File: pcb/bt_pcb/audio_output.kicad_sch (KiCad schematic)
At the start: 37 parts, among them J16 ReanNYS216G, J17 ReanNYS216G, U3 MCP6004

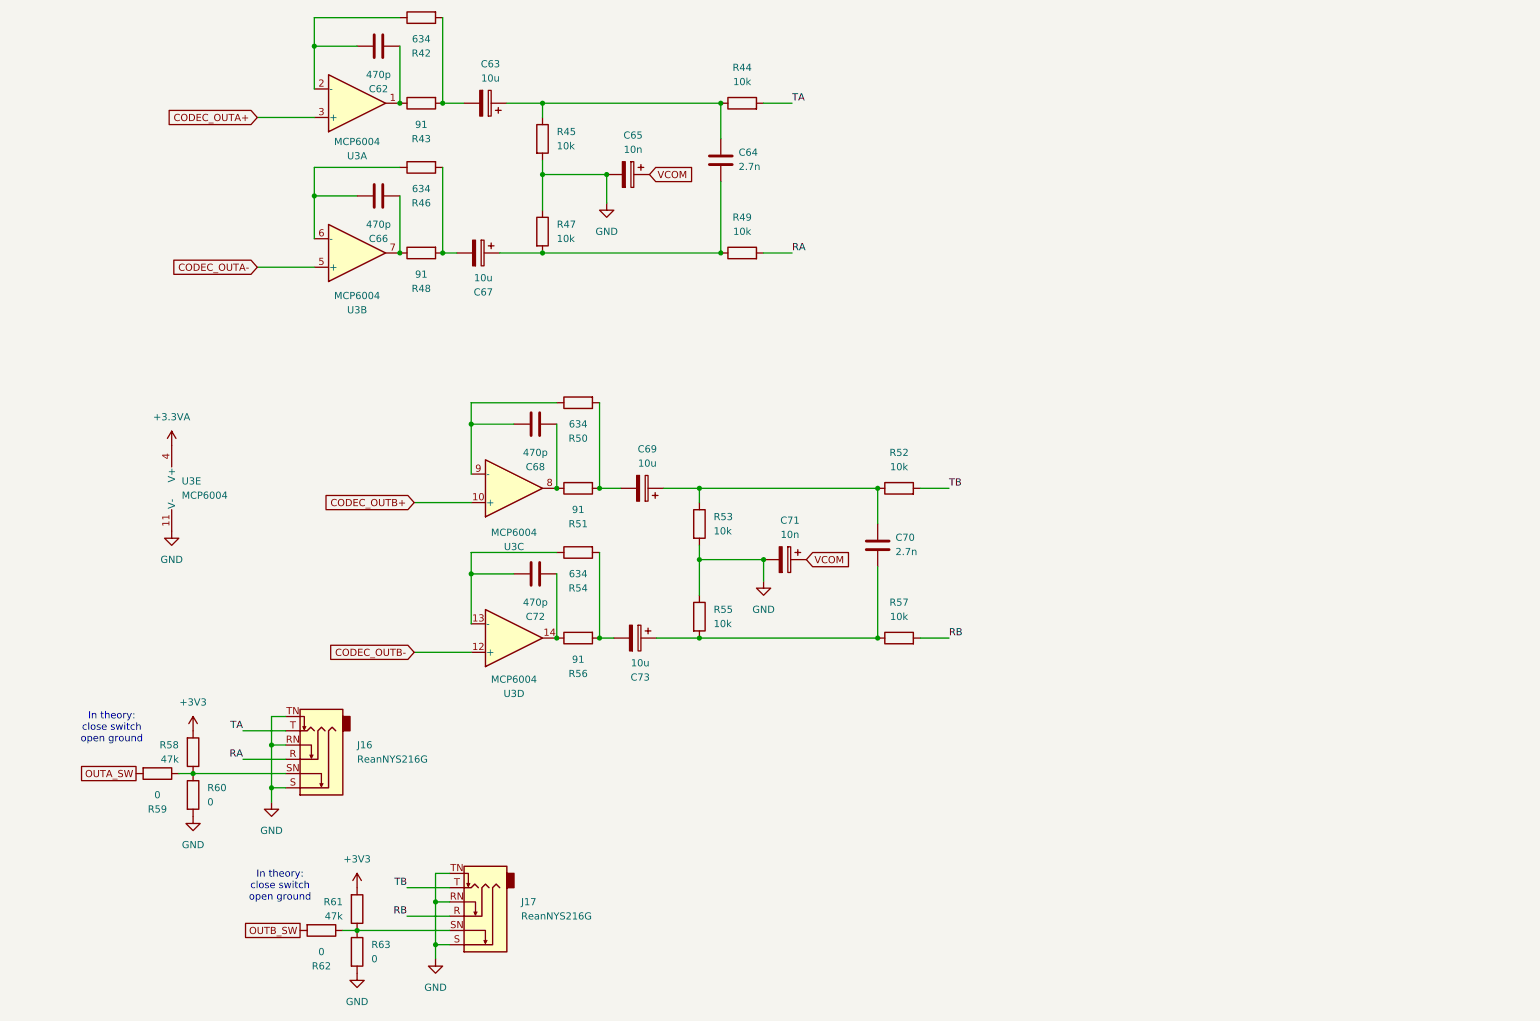
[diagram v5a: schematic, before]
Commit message: pcb with some schematic tuning
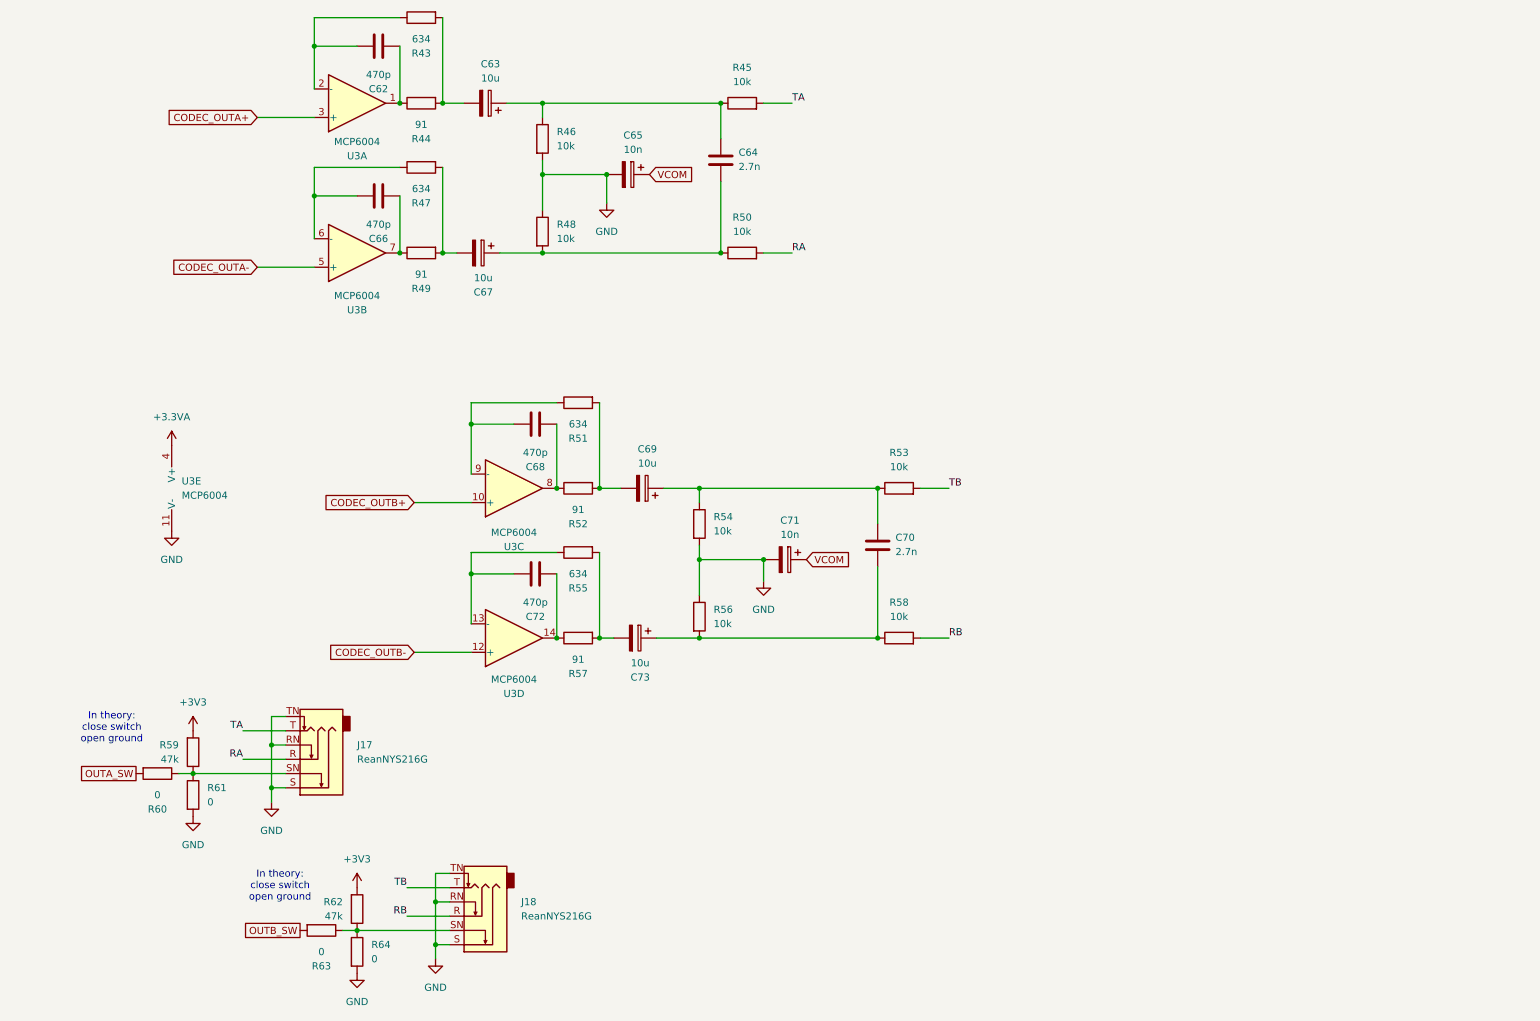
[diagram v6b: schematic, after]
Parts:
- renumbered J16 to J17, J17 to J18, R42 to R43, R43 to R44, R44 to R45, R45 to R46, R46 to R47, R47 to R48, R48 to R49, R49 to R50, R50 to R51, R51 to R52, R52 to R53, R53 to R54, R54 to R55, R55 to R56, R56 to R57, R57 to R58, R58 to R59, R59 to R60, R60 to R61, R61 to R62, R62 to R63, R63 to R64

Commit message: pcb now under revision
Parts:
- R46: renamed from R45; value 10k -> 470
- R51: renamed from R50; value 10k -> 470
- R54: renamed from R53; value 10k -> 470
- R59: renamed from R58; value 10k -> 470
- renumbered C62 to C66, C63 to C67, C64 to C68, C65 to C69, C66 to C70, C67 to C71, C68 to C72, C69 to C73, C70 to C74, C71 to C75, C72 to C76, C73 to C77, R43 to R44, R44 to R45, R46 to R47, R47 to R48, R48 to R49, R49 to R50, R51 to R52, R52 to R53, R54 to R55, R55 to R56, R56 to R57, R57 to R58, R59 to R60, R60 to R61, R61 to R62, R62 to R63, R63 to R64, R64 to R65

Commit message: first notes
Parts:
- renumbered C66 to C56, C67 to C57, C68 to C58, C69 to C59, C70 to C60, C71 to C61, C72 to C62, C73 to C63, C74 to C64, C75 to C65, C76 to C66, C77 to C67, R44 to R45, R45 to R46, R46 to R47, R47 to R48, R48 to R49, R49 to R50, R50 to R51, R51 to R52, R52 to R53, R53 to R54, R54 to R55, R55 to R56, R56 to R57, R57 to R58, R58 to R59, R59 to R60, R60 to R61, R61 to R62, R62 to R63, R63 to R64, R64 to R65, R65 to R66
